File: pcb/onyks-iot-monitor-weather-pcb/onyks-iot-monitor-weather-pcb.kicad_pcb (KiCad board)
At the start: 2 copper layers, 5 parts, among them U1 ESP32-WROOM-32D, U2 AMS1117, U3 AM2302, U6 BMP280, U7 AMS1117

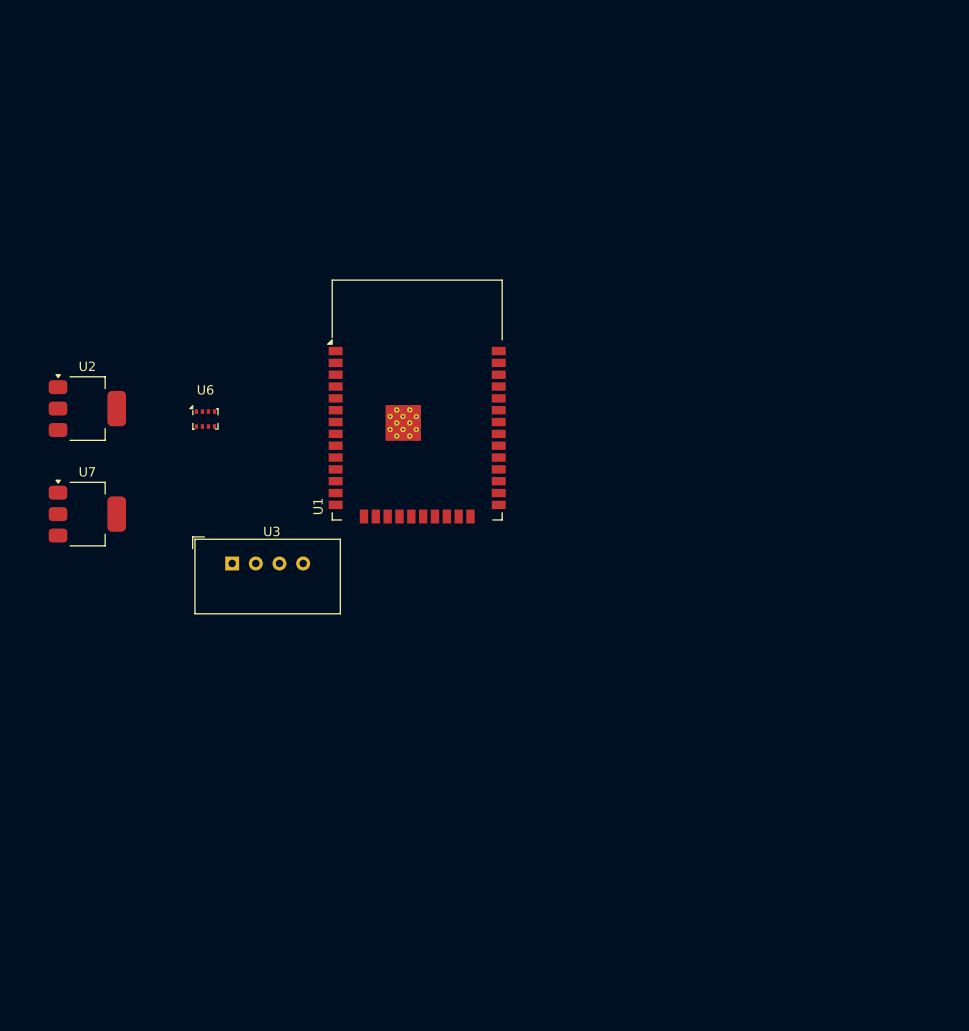
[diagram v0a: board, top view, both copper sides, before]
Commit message: Updated schematics and added footprints and 3dmodels for the elements
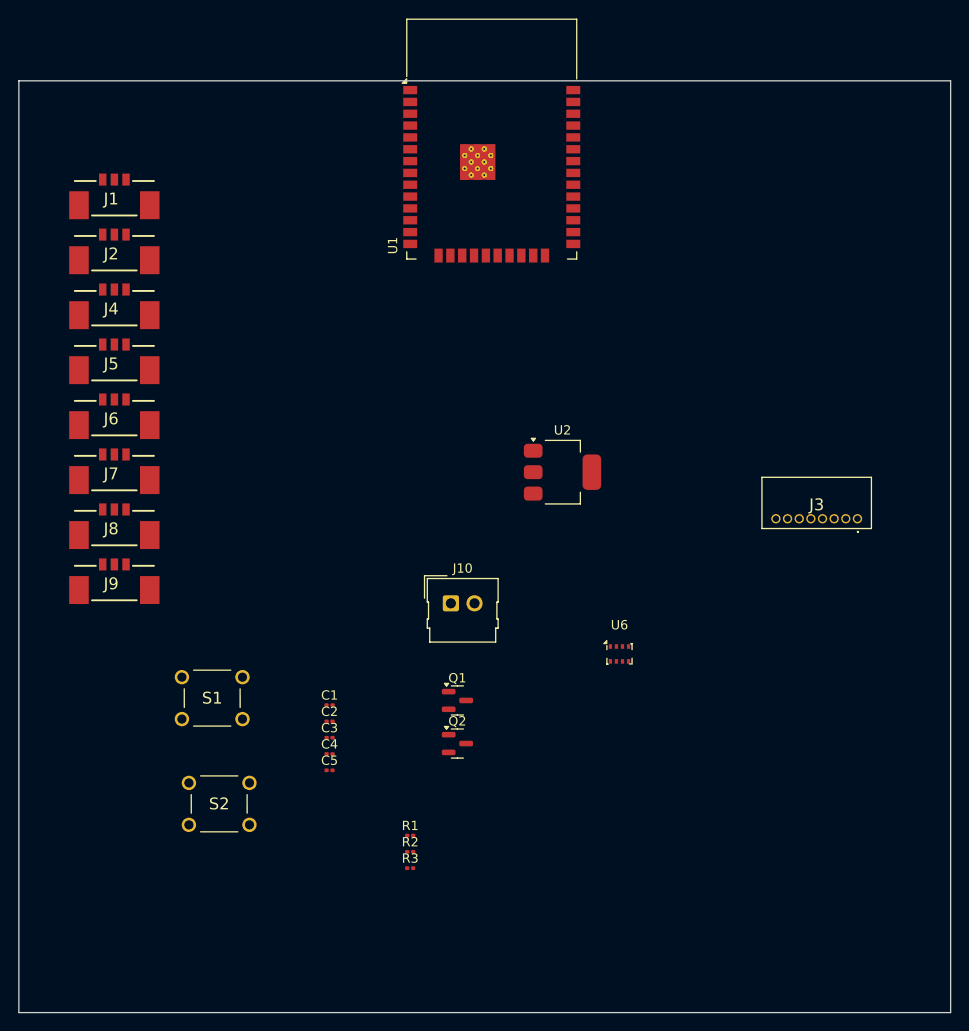
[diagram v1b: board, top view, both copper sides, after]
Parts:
- removed U3: AM2302, Sensor:ASAIR_AM2302_P2.54mm_Vertical
- removed U7: AMS1117, Package_TO_SOT_SMD:SOT-223-3_TabPin2
- added C1: 22uF, Capacitor_SMD:C_0201_0603Metric, F.Cu at (141.8, 123.5)
- added C2: 0.1uF, Capacitor_SMD:C_0201_0603Metric, F.Cu at (141.8, 125.2)
- added C3: 0.1uF, Capacitor_SMD:C_0201_0603Metric, F.Cu at (141.8, 127.0)
- added C4: 0.1uF, Capacitor_SMD:C_0201_0603Metric, F.Cu at (141.8, 128.8)
- added C5: 0.1uF, Capacitor_SMD:C_0201_0603Metric, F.Cu at (141.8, 130.5)
- added J1: 53398-0371, 1bmoje:53398-0371, F.Cu at (118.8, 67.2)
- added J10: Conn_01x02_Pin, Connector_Molex:Molex_SL_171971-0002_1x02_P2.54mm_Vertical, F.Cu at (154.9, 112.6)
- added J2: 53398-0371, 1bmoje:53398-0371, F.Cu at (118.8, 73.2)
- added J3: 53048-0810, 1bmoje:530480810, F.Cu at (198.5, 103.5)
- added J4: 53398-0371, 1bmoje:53398-0371, F.Cu at (118.8, 79.0)
- added J5: 53398-0371, 1bmoje:53398-0371, F.Cu at (118.8, 85.0)
- added J6: 53398-0371, 1bmoje:53398-0371, F.Cu at (118.8, 90.8)
- added J7: 53398-0371, 1bmoje:53398-0371, F.Cu at (118.8, 96.8)
- added J8: 53398-0371, 1bmoje:53398-0371, F.Cu at (118.8, 102.7)
- added J9: 53398-0371, 1bmoje:53398-0371, F.Cu at (118.8, 108.5)
- added Q1: SS8050, Package_TO_SOT_SMD:SOT-23, F.Cu at (155.6, 123.0)
- added Q2: SS8050, Package_TO_SOT_SMD:SOT-23, F.Cu at (155.6, 127.6)
- added R1: 10K, Resistor_SMD:R_0201_0603Metric, F.Cu at (150.5, 137.5)
- added R2: 10K, Resistor_SMD:R_0201_0603Metric, F.Cu at (150.5, 139.2)
- added R3: 10K, Resistor_SMD:R_0201_0603Metric, F.Cu at (150.5, 141.0)
- added S1: BOOT, 1bmoje:18259106, F.Cu at (126.0, 120.5)
- added S2: ENABLE, 1bmoje:18259106, F.Cu at (126.8, 131.8)
- moved U2 51.5 mm to (166.8, 98.5)
- moved U6 51.1 mm to (173.0, 118.0)
- moved U1 29.1 mm to (159.2, 65.7)
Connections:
- U1 pad 10: unconnected-(U1-IO25-Pad10) -> /Hall 1
- U1 pad 11: unconnected-(U1-IO26-Pad11) -> /Hall 2
- U1 pad 12: unconnected-(U1-IO27-Pad12) -> /Hall 3
- U1 pad 13: unconnected-(U1-IO14-Pad13) -> /Hall 6
- U1 pad 2: Net-(U1-VDD) -> /3V3
- U1 pad 6: unconnected-(U1-IO34-Pad6) -> /Hall 5
- U1 pad 8: unconnected-(U1-IO32-Pad8) -> /Hall 4
- U2 pad 2: Net-(U1-VDD) -> /3V3
- U6 pad 2: /BMP_CSB -> /3V3
- U6 pad 6: /BMP_CSB -> /3V3
- U6 pad 8: /BMP_CSB -> /3V3
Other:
- board outline added: 100 x 100 mm
